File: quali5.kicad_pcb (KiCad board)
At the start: 2 copper layers, 91 x 55 mm, 18 parts, among them SW1 SW_PUSH, SW2 SW_PUSH, SW3 SW_PUSH, SW4 SW_PUSH, SW5 SW_PUSH, SW6 SW_PUSH, U1 ProMicro

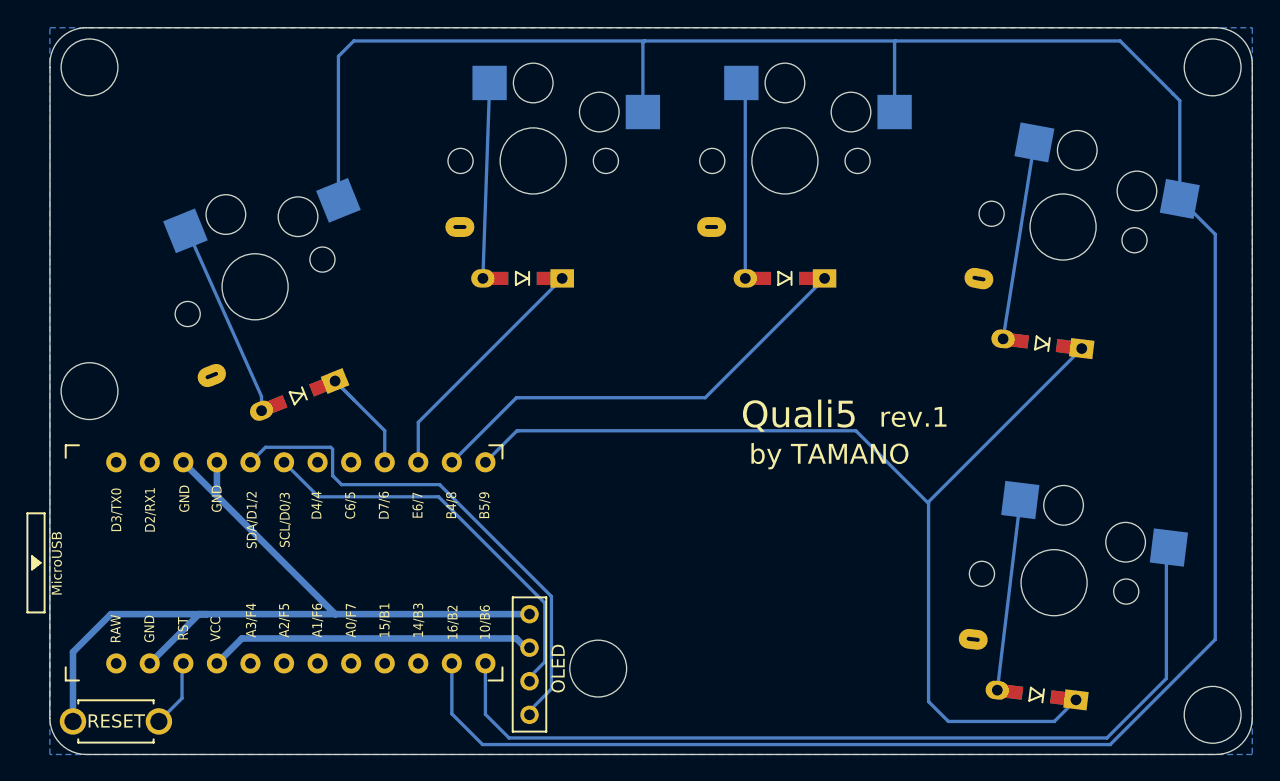
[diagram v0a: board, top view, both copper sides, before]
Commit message: Update PCB for rev.2
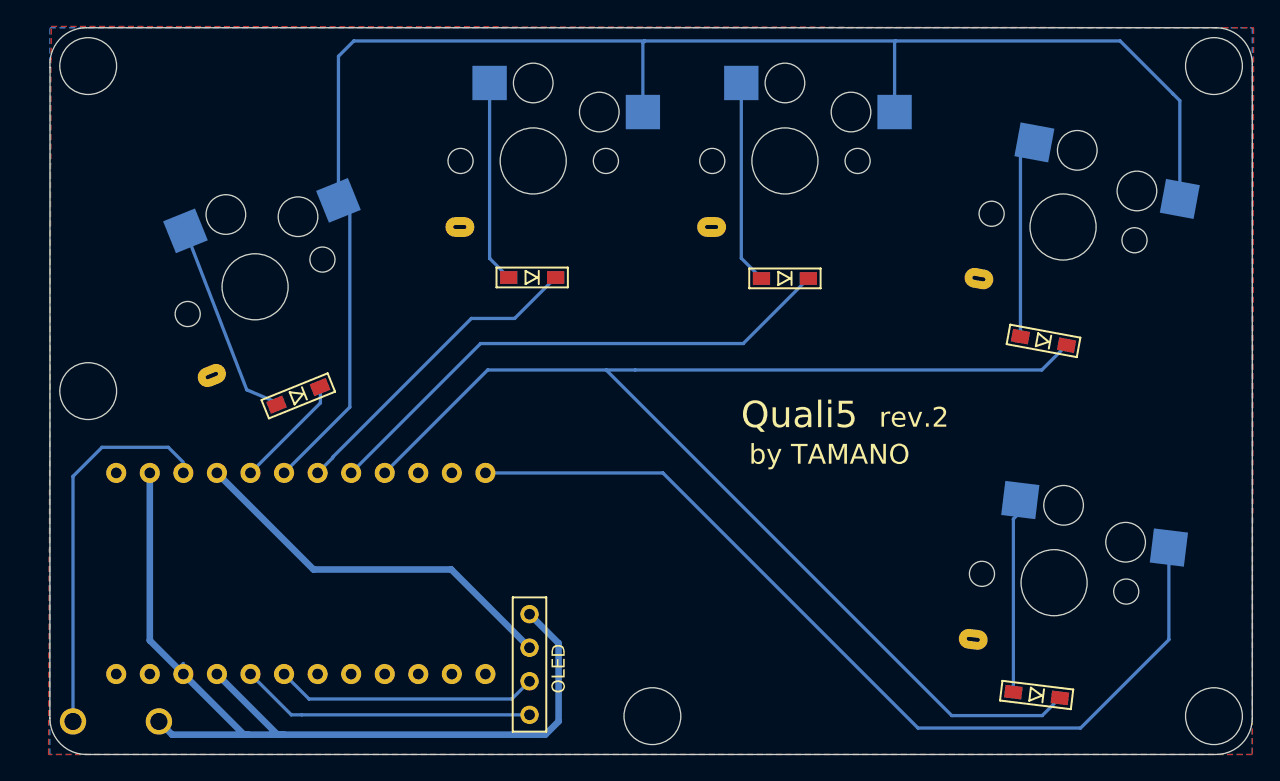
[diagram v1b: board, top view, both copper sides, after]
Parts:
- removed the Ref** at (118.4, 133.6)
- removed the Ref** at (164.9, 137.1)
- removed the Ref** at (164.9, 88.1)
- removed the Ref** at (79.9, 112.6)
- removed the Ref** at (79.9, 88.1)
- added Ref**: Val**, kbd:M2_HOLE_v2, F.Cu at (79.8, 112.6)
- added Ref**: Val**, kbd:M2_HOLE_v2, F.Cu at (122.5, 137.2)
- added Ref**: Val**, kbd:M2_HOLE_v2, F.Cu at (165.0, 137.2)
- added Ref**: Val**, kbd:M2_HOLE_v2, F.Cu at (165.0, 88.0)
- added Ref**: Val**, kbd:M2_HOLE_v2, F.Cu at (79.8, 88.0)
- D1, D2, D3, D4, D5: footprint kbd:D3_TH -> kbd:D3_SMD; moved to B.Cu
- SW1, U1: moved to B.Cu
- moved U1 0.80 mm to (96.4, 126.4), turned to 270 degrees
- moved D2 0.73 mm to (113.4, 104.0)
- moved D4 0.23 mm to (152.1, 108.8), turned to 169.5 degrees
- turned SW1 to 180 degrees
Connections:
- U1 pad 10: row1 -> (no net)
- U1 pad 11: row2 -> (no net)
- U1 pad 12: row3 -> (no net)
- U1 pad 14: col0 -> (no net)
- U1 pad 16: (no net) -> row3
- U1 pad 17: (no net) -> row2
- U1 pad 18: (no net) -> row1
- U1 pad 19: (no net) -> col0
- U1 pad 20: (no net) -> row0
- U1 pad 9: row0 -> (no net)
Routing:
- net col0: track 195.5 -> 118.3 mm
- net RST: track 5.16 -> 28.3 mm
- net row3: track 80.8 -> 101.3 mm
- net SDA: track 38.9 -> 22.4 mm
- net SCL: track 30.7 -> 19.9 mm
- net row2: track 34.0 -> 40.7 mm
- net row1: track 18.4 -> 24.2 mm
- net GND: track 65.3 -> 70.3 mm
- net VCC: track 24.4 -> 29.1 mm
- net col1: track 68.0 -> 69.7 mm
- net row0: track 9.72 -> 8.70 mm
- net Net-(D3-Pad2): track 14.9 -> 15.8 mm
- net Net-(D1-Pad2): track 14.9 -> 15.7 mm
- net Net-(D2-Pad2): track 14.8 -> 15.4 mm
- added copper zone on F.Cu, net GND
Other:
- board text added: "rev.2"
- board text removed: "rev.1"
